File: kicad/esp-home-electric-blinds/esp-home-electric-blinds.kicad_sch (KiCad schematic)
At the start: 4 parts, among them J1 AC_IN

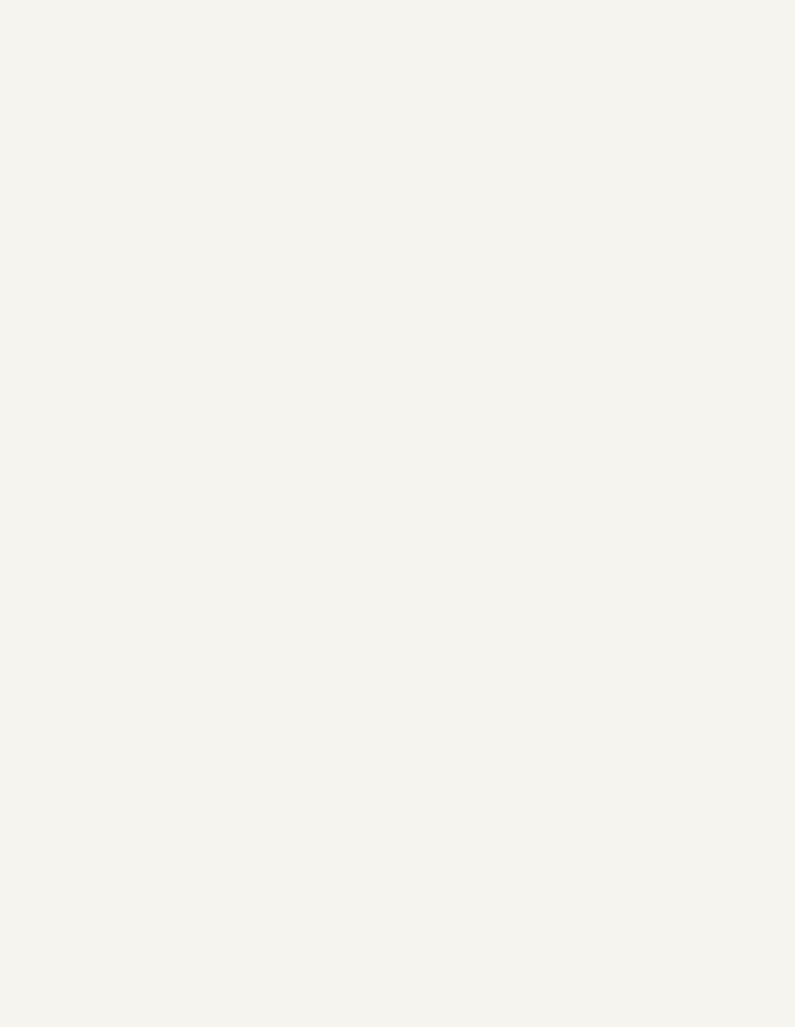
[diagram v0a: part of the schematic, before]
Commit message: esp32 added
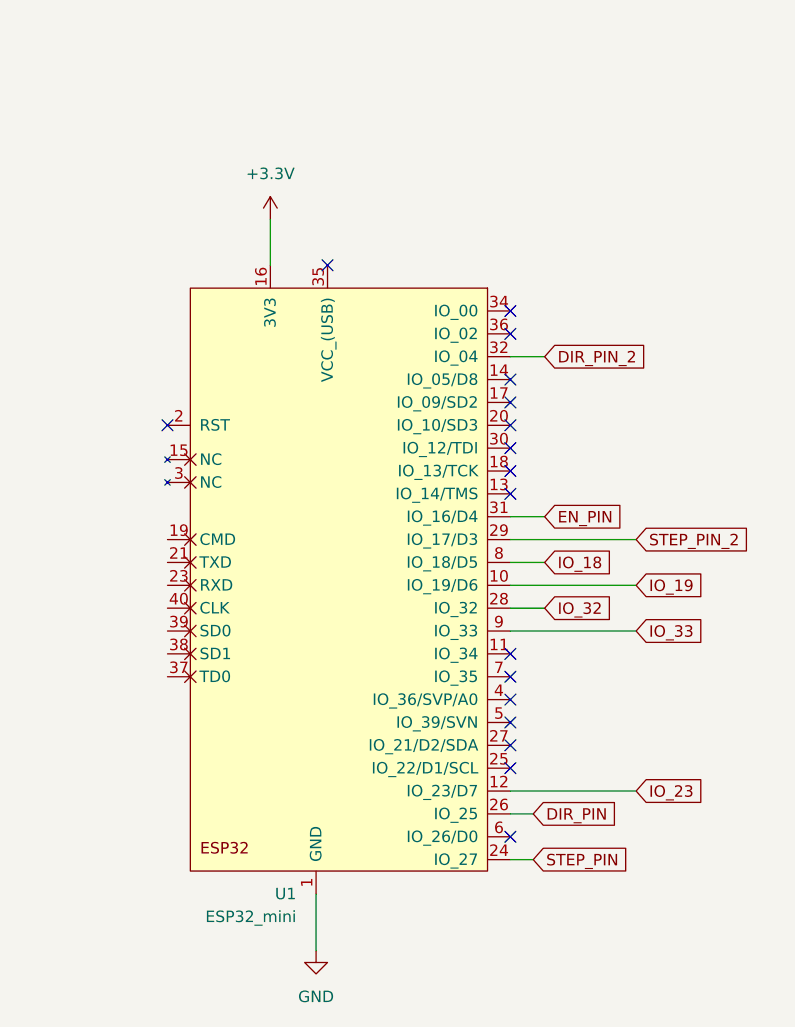
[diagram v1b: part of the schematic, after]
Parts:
- added U1: ESP32_mini, microcontrollers_johnymalina:ESP32_mini, symbol johnymalina_microcontrollers:ESP32_mini
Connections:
- net +3.3V: now also U1.16 (3V3)
- net GND: now also U1.1 (GND), U1.22 (GND), U1.33 (GND)
- new net DIR_PIN: U1.26 (IO_25)
- new net DIR_PIN_2: U1.32 (IO_04)
- new net EN_PIN: U1.31 (IO_16/D4)
- new net IO_18: U1.8 (IO_18/D5)
- new net IO_19: U1.10 (IO_19/D6)
- new net IO_23: U1.12 (IO_23/D7)
- new net IO_32: U1.28 (IO_32)
- new net IO_33: U1.9 (IO_33)
- new net STEP_PIN: U1.24 (IO_27)
- new net STEP_PIN_2: U1.29 (IO_17/D3)
- no-connect marks 0 -> 17

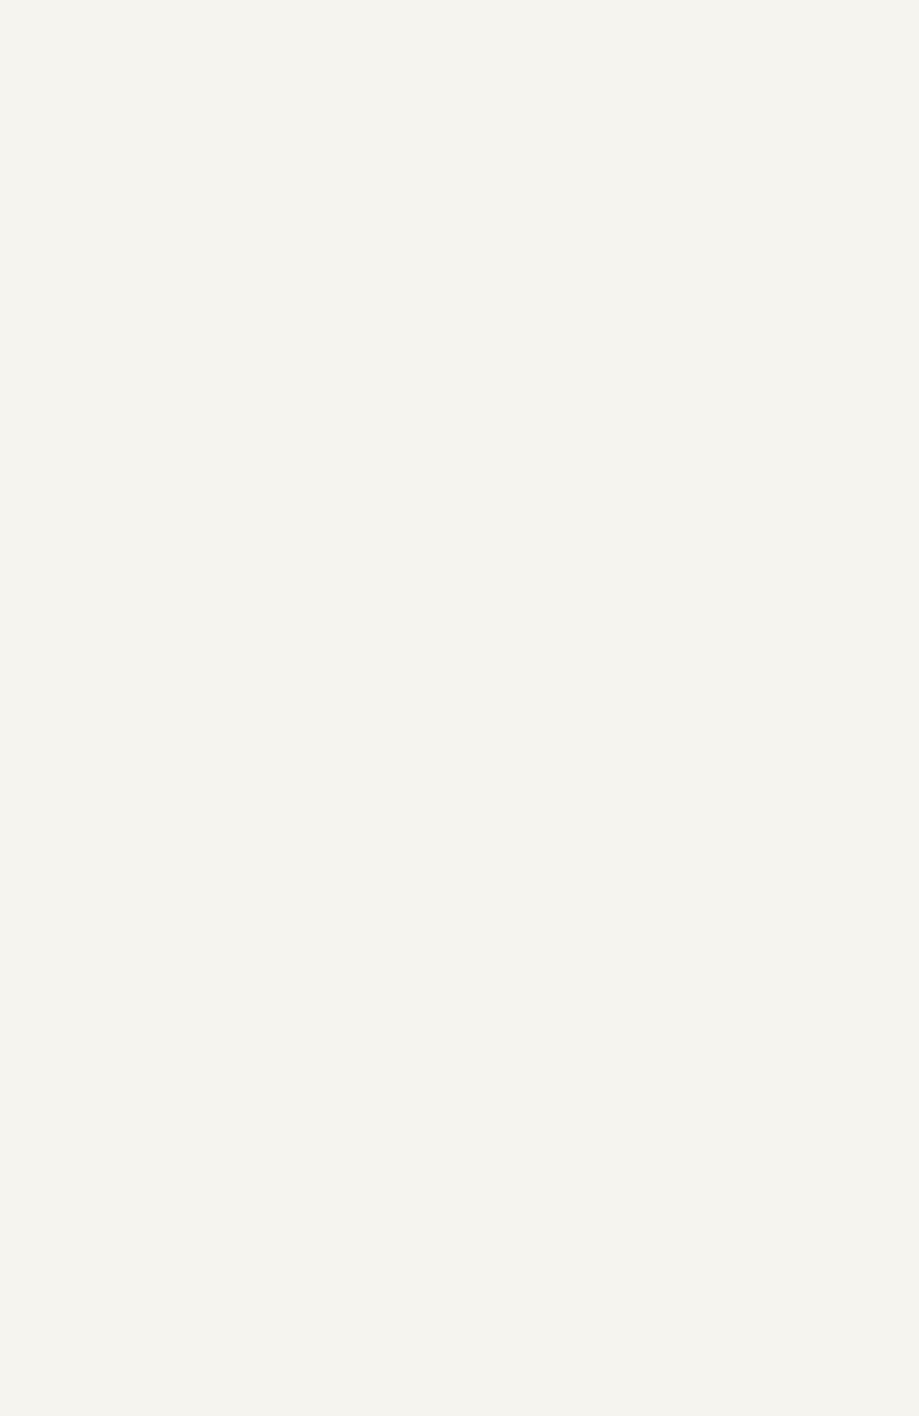
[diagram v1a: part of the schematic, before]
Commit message: added steppers
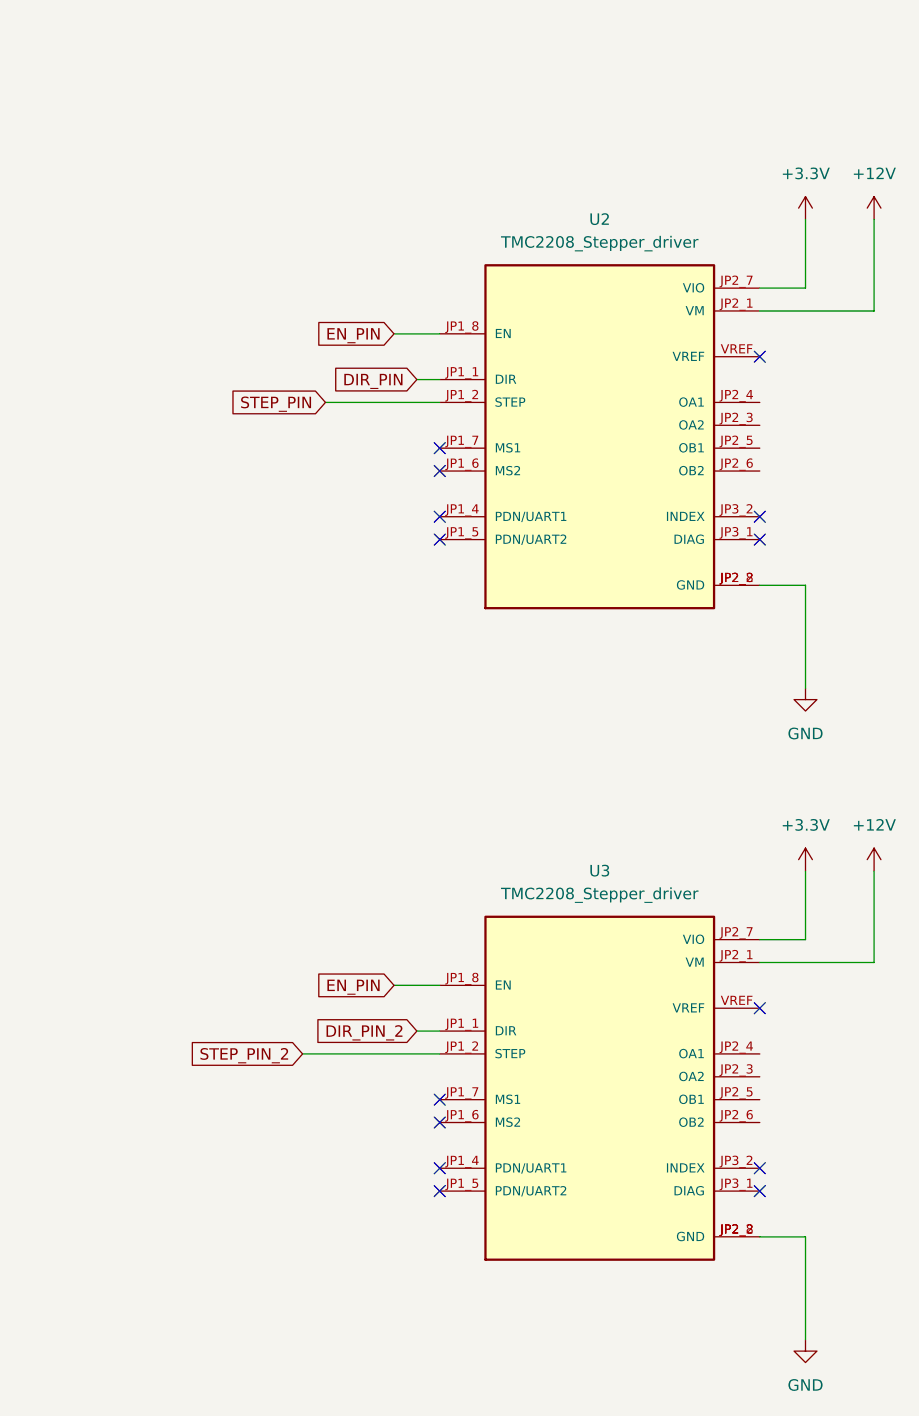
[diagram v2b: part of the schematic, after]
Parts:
- added U2, U3: TMC2208_Stepper_driver, MODULE_TMC2208_SILENTSTEPSTICK, symbol johnymalina_components:TMC2208_Stepper_driver
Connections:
- net +12V: now also U2.JP2_1 (VM), U3.JP2_1 (VM)
- net +3.3V: now also U2.JP2_7 (VIO), U3.JP2_7 (VIO)
- net DIR_PIN: now also U2.JP1_1 (DIR)
- net DIR_PIN_2: now also U3.JP1_1 (DIR)
- net EN_PIN: now also U2.JP1_8 (EN), U3.JP1_8 (EN)
- net GND: now also U2.JP2_2 (GND), U2.JP2_8 (GND), U3.JP2_2 (GND), U3.JP2_8 (GND)
- net STEP_PIN: now also U2.JP1_2 (STEP)
- net STEP_PIN_2: now also U3.JP1_2 (STEP)
- no-connect marks 17 -> 31

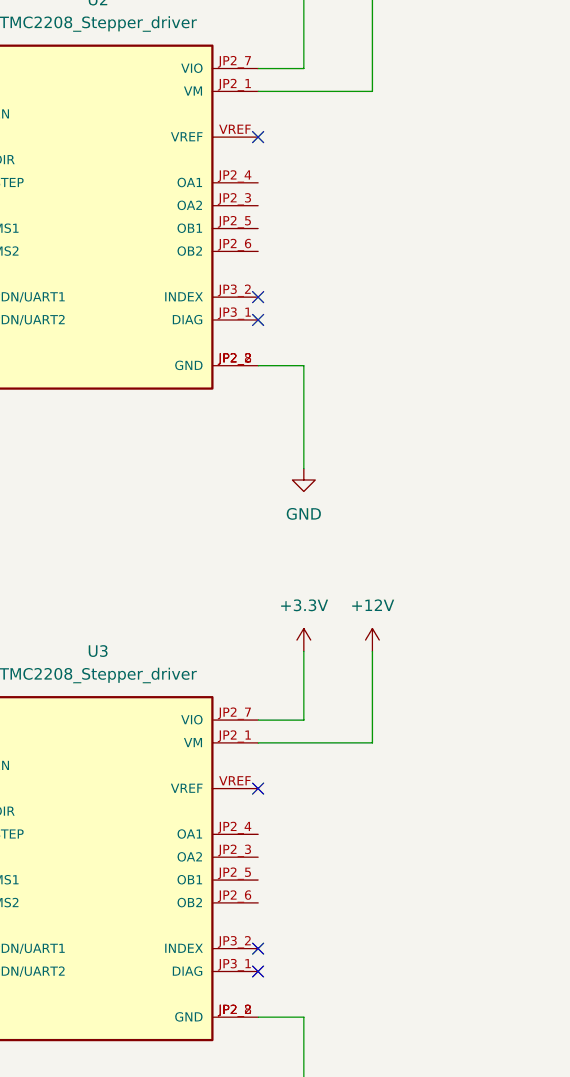
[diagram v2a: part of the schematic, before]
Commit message: added stepper connector
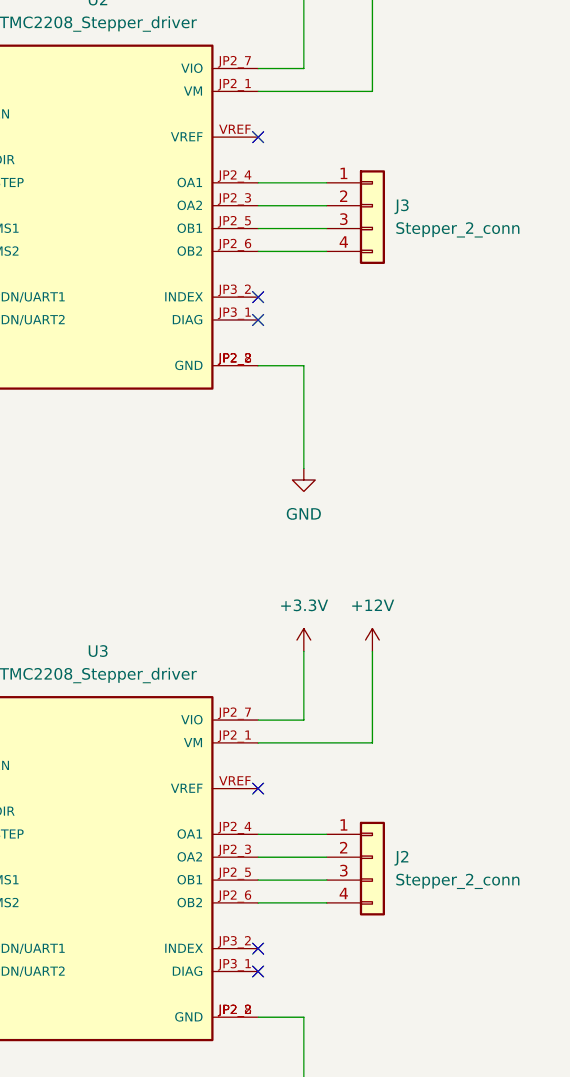
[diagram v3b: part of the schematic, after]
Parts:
- added J2, J3: Stepper_2_conn, symbol Connector_Generic:Conn_01x04
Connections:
- net at U2.JP2_3 (OA2): now also J3.2 (Pin_2)
- net at U2.JP2_4 (OA1): now also J3.1 (Pin_1)
- net at U2.JP2_5 (OB1): now also J3.3 (Pin_3)
- net at U2.JP2_6 (OB2): now also J3.4 (Pin_4)
- net at U3.JP2_3 (OA2): now also J2.2 (Pin_2)
- net at U3.JP2_4 (OA1): now also J2.1 (Pin_1)
- net at U3.JP2_5 (OB1): now also J2.3 (Pin_3)
- net at U3.JP2_6 (OB2): now also J2.4 (Pin_4)
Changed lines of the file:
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@@
+	(wire
+		(pts
+			(xy 228.6 100.33) (xy 220.98 100.33)
+		)
+		(stroke
+			(width 0)
+			(type default)
+		)
+	)
 	(wire
 		(pts
@@
 	(wire
 		(pts
+			(xy 228.6 105.41) (xy 220.98 105.41)
+		)
+		(stroke
+			(width 0)
+			(type default)
+		)
+	)
+	(wire
+		(pts
 			(xy 226.06 118.11) (xy 226.06 129.54)
 		)
@@
 	(wire
 		(pts
+			(xy 228.6 172.72) (xy 220.98 172.72)
+		)
+		(stroke
+			(width 0)
+			(type default)
+		)
+	)
+	(wire
+		(pts
 			(xy 182.88 167.64) (xy 185.42 167.64)
 		)
@@
 	(wire
 		(pts
+			(xy 228.6 102.87) (xy 220.98 102.87)
+		)
+		(stroke
+			(width 0)
+			(type default)
+		)
+	)
+	(wire
+		(pts
 			(xy 109.22 38.1) (xy 114.3 38.1)
 		)
@@
 	(wire
 		(pts
+			(xy 228.6 170.18) (xy 220.98 170.18)
+		)
+		(stroke
+			(width 0)
+			(type default)
+		)
+	)
+	(wire
+		(pts
 			(xy 96.52 138.43) (xy 92.71 138.43)
 		)
@@
 	(wire
 		(pts
+			(xy 228.6 97.79) (xy 220.98 97.79)
+		)
+		(stroke
+			(width 0)
+			(type default)
+		)
+	)
+	(wire
+		(pts
+			(xy 228.6 177.8) (xy 220.98 177.8)
+		)
+		(stroke
+			(width 0)
+			(type default)
+		)
+	)
+	(wire
+		(pts
 			(xy 67.31 38.1) (xy 88.9 38.1)
 		)
@@
 		(pts
 			(xy 233.68 87.63) (xy 220.98 87.63)
+		)
+		(stroke
+			(width 0)
+			(type default)
+		)
+	)
+	(wire
+		(pts
+			(xy 228.6 175.26) (xy 220.98 175.26)
 		)
 		(stroke
@@
 	)
 	(symbol
+		(lib_id "Connector_Generic:Conn_01x04")
+		(at 233.68 100.33 0)
+		(unit 1)
+		(exclude_from_sim no)
+		(in_bom yes)
+		(on_board yes)
+		(dnp no)
+		(fields_autoplaced yes)
+		(property "Reference" "J3"
+			(at 236.22 100.3299 0)
+			(effects
+				(font
+					(size 1.27 1.27)
+				)
+				(justify left)
+			)
+		)
+		(property "Value" "Stepper_2_conn"
+			(at 236.22 102.8699 0)
+			(effects
+				(font
+					(size 1.27 1.27)
+				)
+				(justify left)
+			)
+		)
+		(property "Footprint" ""
+			(at 233.68 100.33 0)
+			(effects
+				(font
+					(size 1.27 1.27)
+				)
+				(hide yes)
+			)
+		)
+		(property "Datasheet" "~"
+			(at 233.68 100.33 0)
+			(effects
+				(font
+					(size 1.27 1.27)
+				)
+				(hide yes)
+			)
+		)
+		(property "Description" "Generic connector, single row, 01x04, script generated (kicad-library-utils/schlib/autogen/connector/)"
+			(at 233.68 100.33 0)
+			(effects
+				(font
+					(size 1.27 1.27)
+				)
+				(hide yes)
+			)
+		)
+		(pin "2"
+		)
+		(pin "3"
+		)
+		(pin "4"
+		)
+		(pin "1"
+		)
+		(instances
+			(project "esp-home-electric-blinds"
+				(path "/07d3a4e0-56e5-4d89-afd4-c6828a783612"
+					(reference "J3")
+					(unit 1)
+				)
+			)
+		)
+	)
+	(symbol
 		(lib_id "Device:Fuse")
 		(at 77.47 33.02 90)
@@
 					(unit 1)
 				)
+			)
+		)
+	)
+	(symbol
+		(lib_id "Connector_Generic:Conn_01x04")
+		(at 233.68 172.72 0)
+		(unit 1)
+		(exclude_from_sim no)
+		(in_bom yes)
+		(on_board yes)
+		(dnp no)
+		(fields_autoplaced yes)
+		(property "Reference" "J2"
+			(at 236.22 172.7199 0)
+			(effects
+				(font
+					(size 1.27 1.27)
+				)
+				(justify left)
+			)
+		)
+		(property "Value" "Stepper_2_conn"
+			(at 236.22 175.2599 0)
+			(effects
+				(font
+					(size 1.27 1.27)
+				)
+				(justify left)
+			)
+		)
+		(property "Footprint" ""
+			(at 233.68 172.72 0)
+			(effects
+				(font
+					(size 1.27 1.27)
+				)
+				(hide yes)
+			)
+		)
+		(property "Datasheet" "~"
+			(at 233.68 172.72 0)
+			(effects
+				(font
+					(size 1.27 1.27)
+				)
+				(hide yes)
+			)
+		)
+		(property "Description" "Generic connector, single row, 01x04, script generated (kicad-library-utils/schlib/autogen/connector/)"
+			(at 233.68 172.72 0)
+			(effects
+				(font
+					(size 1.27 1.27)
+				)
+				(hide yes)
+			)
+		)
+		(pin "2"
+		)
+		(pin "3"
+		)
+		(pin "4"
+		)
+		(pin "1"
+		)
+		(instances
+			(project "esp-home-electric-blinds"
+				(path "/07d3a4e0-56e5-4d89-afd4-c6828a783612"
+					(reference "J2")
+					(unit 1)
+				)

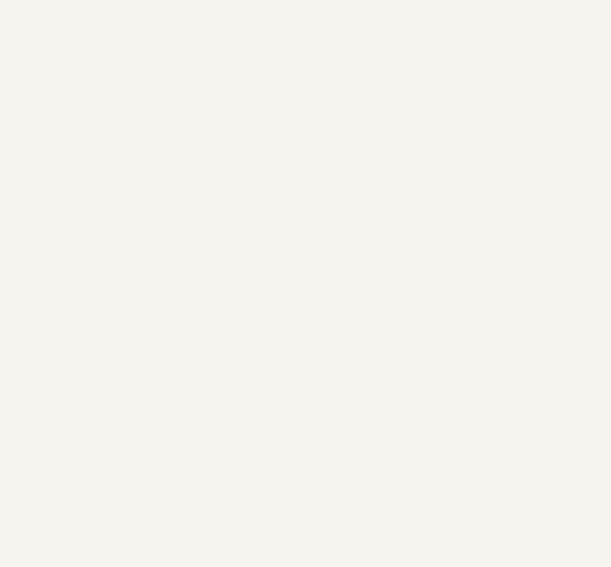
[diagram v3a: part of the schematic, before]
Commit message: added IO connector
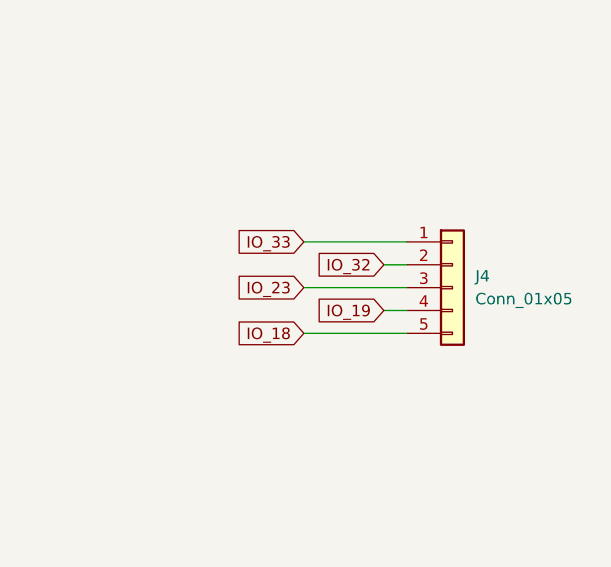
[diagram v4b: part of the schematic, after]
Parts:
- added J4: Conn_01x05, symbol Connector_Generic:Conn_01x05
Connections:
- net IO_18: now also J4.5 (Pin_5)
- net IO_19: now also J4.4 (Pin_4)
- net IO_23: now also J4.3 (Pin_3)
- net IO_32: now also J4.2 (Pin_2)
- net IO_33: now also J4.1 (Pin_1)
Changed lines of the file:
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@@
+	(wire
+		(pts
+			(xy 312.42 139.7) (xy 323.85 139.7)
+		)
+		(stroke
+			(width 0)
+			(type default)
+		)
+	)
 	(wire
 		(pts
@@
 	(wire
 		(pts
+			(xy 312.42 149.86) (xy 323.85 149.86)
+		)
+		(stroke
+			(width 0)
+			(type default)
+		)
+	)
+	(wire
+		(pts
 			(xy 233.68 149.86) (xy 233.68 160.02)
 		)
@@
 	(wire
 		(pts
+			(xy 321.31 142.24) (xy 323.85 142.24)
+		)
+		(stroke
+			(width 0)
+			(type default)
+		)
+	)
+	(wire
+		(pts
 			(xy 109.22 33.02) (xy 114.3 33.02)
 		)
@@
 	(wire
 		(pts
+			(xy 312.42 144.78) (xy 323.85 144.78)
+		)
+		(stroke
+			(width 0)
+			(type default)
+		)
+	)
+	(wire
+		(pts
 			(xy 43.18 36.83) (xy 43.18 38.1)
 		)
@@
 	(wire
 		(pts
+			(xy 321.31 147.32) (xy 323.85 147.32)
+		)
+		(stroke
+			(width 0)
+			(type default)
+		)
+	)
+	(wire
+		(pts
 			(xy 67.31 38.1) (xy 88.9 38.1)
 		)
@@
 		)
 	)
+	(global_label "IO_19"
+		(shape input)
+		(at 321.31 147.32 180)
+		(fields_autoplaced yes)
+		(effects
+			(font
+				(size 1.27 1.27)
+			)
+			(justify right)
+		)
+		(property "Intersheetrefs" "${INTERSHEET_REFS}"
+			(at 313.0029 147.32 0)
+			(effects
+				(font
+					(size 1.27 1.27)
+				)
+				(justify right)
+				(hide yes)
+			)
+		)
+	)
 	(global_label "IO_18"
 		(shape input)
+		(at 312.42 149.86 180)
+		(fields_autoplaced yes)
+		(effects
+			(font
+				(size 1.27 1.27)
+			)
+			(justify right)
+		)
+		(property "Intersheetrefs" "${INTERSHEET_REFS}"
+			(at 304.1129 149.86 0)
+			(effects
+				(font
+					(size 1.27 1.27)
+				)
+				(justify right)
+				(hide yes)
+			)
+		)
+	)
+	(global_label "IO_18"
+		(shape input)
 		(at 96.52 133.35 0)
 		(fields_autoplaced yes)
@@
 		)
 	)
+	(global_label "IO_32"
+		(shape input)
+		(at 321.31 142.24 180)
+		(fields_autoplaced yes)
+		(effects
+			(font
+				(size 1.27 1.27)
+			)
+			(justify right)
+		)
+		(property "Intersheetrefs" "${INTERSHEET_REFS}"
+			(at 313.0029 142.24 0)
+			(effects
+				(font
+					(size 1.27 1.27)
+				)
+				(justify right)
+				(hide yes)
+			)
+		)
+	)
 	(global_label "STEP_PIN"
 		(shape input)
@@
 		)
 	)
+	(global_label "IO_23"
+		(shape input)
+		(at 312.42 144.78 180)
+		(fields_autoplaced yes)
+		(effects
+			(font
+				(size 1.27 1.27)
+			)
+			(justify right)
+		)
+		(property "Intersheetrefs" "${INTERSHEET_REFS}"
+			(at 304.1129 144.78 0)
+			(effects
+				(font
+					(size 1.27 1.27)
+				)
+				(justify right)
+				(hide yes)
+			)
+		)
+	)
 	(global_label "STEP_PIN_2"
 		(shape input)
@@
 				)
 				(justify left)
+				(hide yes)
+			)
+		)
+	)
+	(global_label "IO_33"
+		(shape input)
+		(at 312.42 139.7 180)
+		(fields_autoplaced yes)
+		(effects
+			(font
+				(size 1.27 1.27)
+			)
+			(justify right)
+		)
+		(property "Intersheetrefs" "${INTERSHEET_REFS}"
+			(at 304.1129 139.7 0)
+			(effects
+				(font
+					(size 1.27 1.27)
+				)
+				(justify right)
 				(hide yes)
 			)
@@
 					(unit 1)
 				)
+			)
+		)
+	)
+	(symbol
+		(lib_id "Connector_Generic:Conn_01x05")
+		(at 328.93 144.78 0)
+		(unit 1)
+		(exclude_from_sim no)
+		(in_bom yes)
+		(on_board yes)
+		(dnp no)
+		(fields_autoplaced yes)
+		(property "Reference" "J4"
+			(at 331.47 143.5099 0)
+			(effects
+				(font
+					(size 1.27 1.27)
+				)
+				(justify left)
+			)
+		)
+		(property "Value" "Conn_01x05"
+			(at 331.47 146.0499 0)
+			(effects
+				(font
+					(size 1.27 1.27)
+				)
+				(justify left)
+			)
+		)
+		(property "Footprint" ""
+			(at 328.93 144.78 0)
+			(effects
+				(font
+					(size 1.27 1.27)
+				)
+				(hide yes)
+			)
+		)
+		(property "Datasheet" "~"
+			(at 328.93 144.78 0)
+			(effects
+				(font
+					(size 1.27 1.27)
+				)
+				(hide yes)
+			)
+		)
+		(property "Description" "Generic connector, single row, 01x05, script generated (kicad-library-utils/schlib/autogen/connector/)"
+			(at 328.93 144.78 0)
+			(effects
+				(font
+					(size 1.27 1.27)
+				)
+				(hide yes)
+			)
+		)
+		(pin "5"
+		)
+		(pin "3"
+		)
+		(pin "4"
+		)
+		(pin "1"
+		)
+		(pin "2"
+		)
+		(instances
+			(project "esp-home-electric-blinds"
+				(path "/07d3a4e0-56e5-4d89-afd4-c6828a783612"
+					(reference "J4")
+					(unit 1)
+				)

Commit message: rearange
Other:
- note added: "ESP32 Mini"
- note added: "IO Connector"
- note added: "Power"
- note added: "Stepper Motors"
- moved on the sheet: F1, J1, J2, J3, J4, PS1, PS2, U1, U2, U3
